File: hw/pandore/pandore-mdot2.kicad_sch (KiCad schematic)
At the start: 15 parts, among them J13 NGFF_M.2_M, J19 NGFF_M.2_AE, M2AE30 M2, M2M110 M2, M2M42 M2, M2M60 M2, M2M80 M2

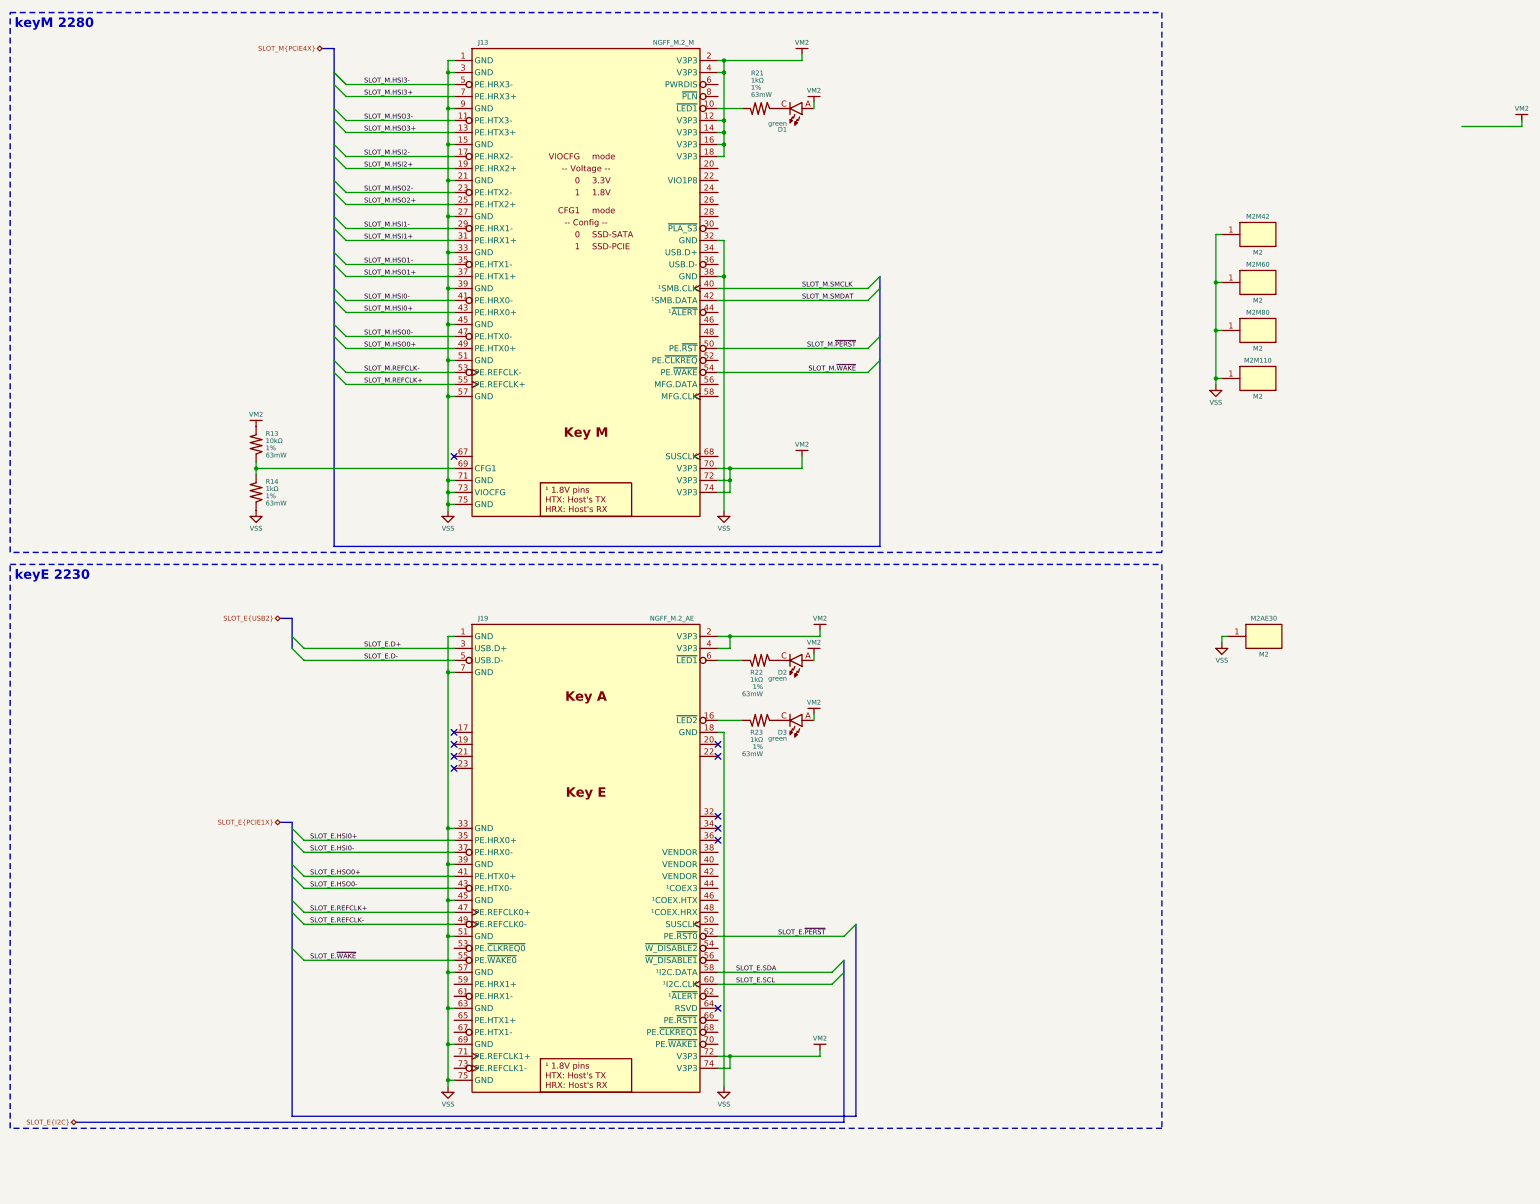
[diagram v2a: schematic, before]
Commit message: most of board control signals added, routed and defined
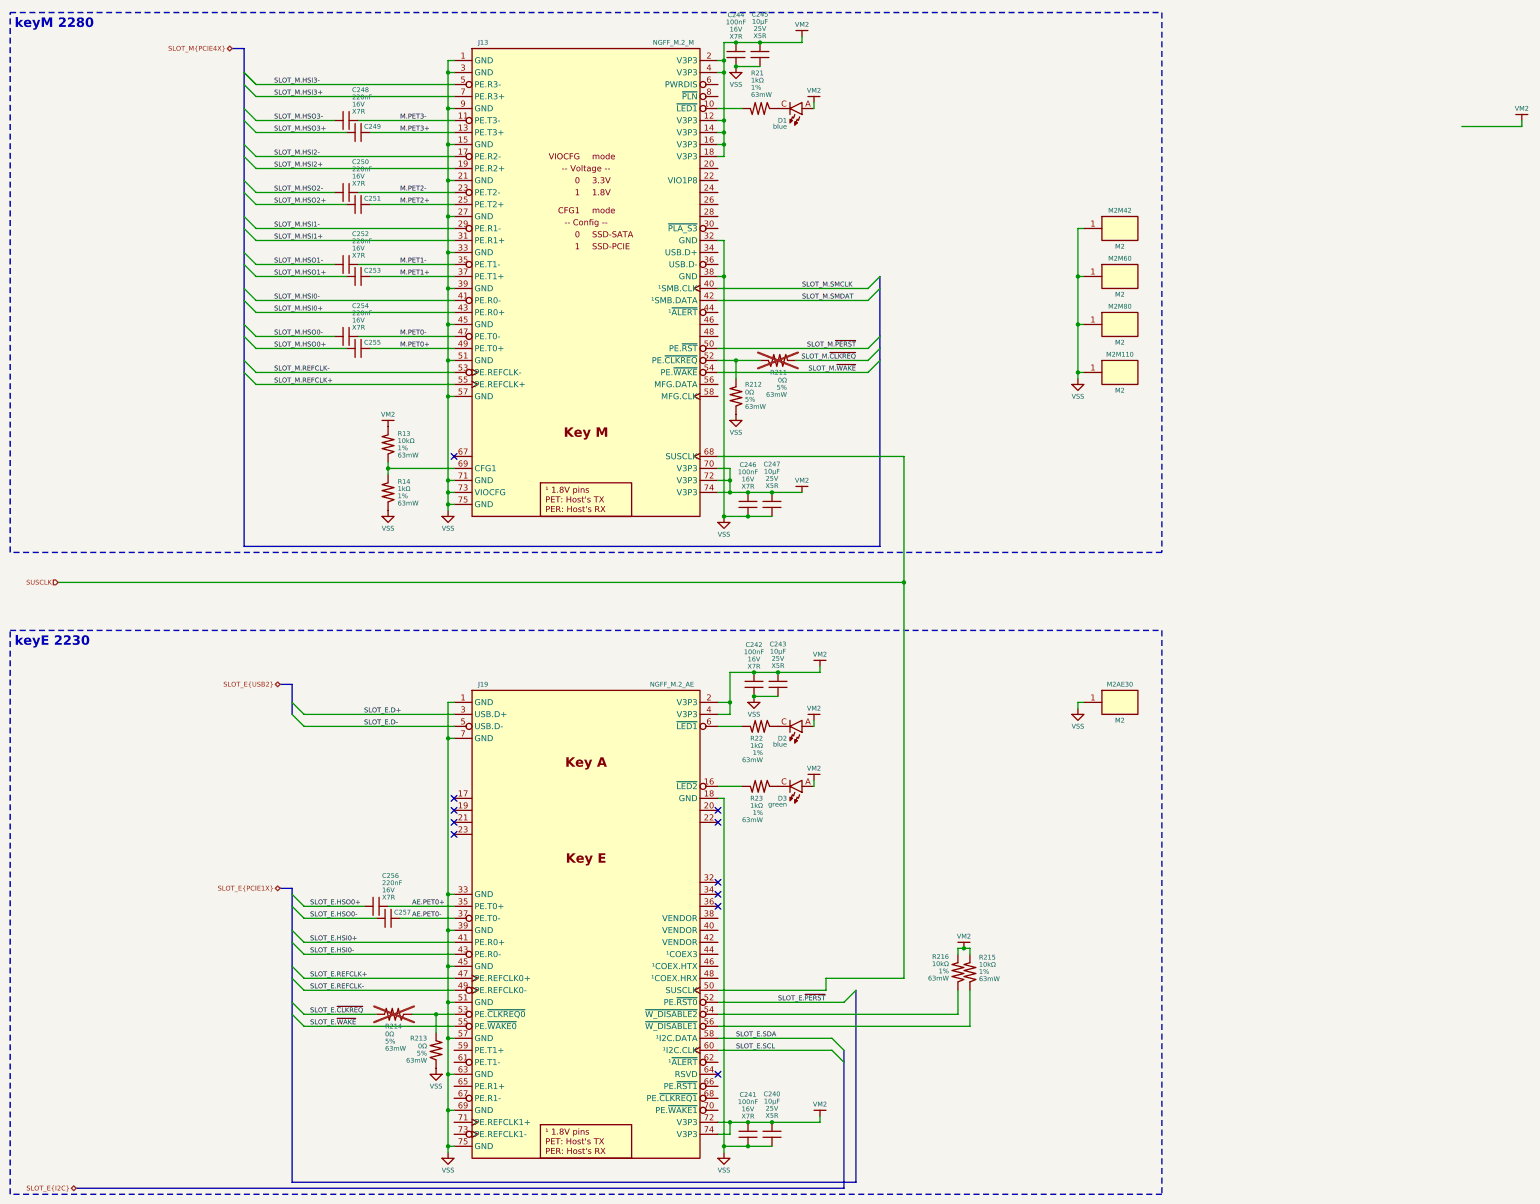
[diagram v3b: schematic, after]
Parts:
- added C240, C243, C245, C247: ${Capacitance}, ${Voltage}, ${Dielectric}, reekilib_cap:CAPC2012, symbol reekilib_cap:cap
- added C241, C242, C244, C246, C248, C249, C250, C251, C252, C253, C254, C255, C256, C257: ${Capacitance}, ${Voltage}, ${Dielectric}, reekilib_cap:CAPC1005, symbol reekilib_cap:cap
- added R211, R212, R213, R214, R215, R216: ${Resistance}, ${Tolerance}, ${Power}, reekilib_res:RESC1005, symbol reekilib_res:res
- D1, D2: Imax 30mA -> 25mA; Link https://ams-osram.com/products/leds/color-leds/osram-smartled-0603-kt-eelp41-12 -> https://ams-osram.com/products/leds/color-leds/osram-smartled-0603-kb-eelp41-12; MPN KT EELP41.12-S2U1-25-2X4Y -> KB EELP41.12-P1R2-36-3X4X; Vf 2.5V -> 2.75V; color green -> blue; lum 224mcd@5mA -> 112mcd@5mA; λdom 527nm -> 470nm
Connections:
- net SLOT_E.HSI0+: now also J19.41 (PE.R0+); no longer J19.35 (PE.HRX0+)
- net SLOT_E.HSI0-: now also J19.43 (PE.R0-); no longer J19.37 (PE.HRX0-)
- net SLOT_E.HSO0+: now also C256.2; no longer J19.41 (PE.HTX0+)
- net SLOT_E.HSO0-: now also C257.2; no longer J19.43 (PE.HTX0-)
- net SLOT_M.HSO0+: now also C255.2; no longer J13.49 (PE.HTX0+)
- net SLOT_M.HSO0-: now also C254.2; no longer J13.47 (PE.HTX0-)
- net SLOT_M.HSO1+: now also C253.2; no longer J13.37 (PE.HTX1+)
- net SLOT_M.HSO1-: now also C252.2; no longer J13.35 (PE.HTX1-)
- net SLOT_M.HSO2+: now also C251.2; no longer J13.25 (PE.HTX2+)
- net SLOT_M.HSO2-: now also C250.2; no longer J13.23 (PE.HTX2-)
- net SLOT_M.HSO3+: now also C249.2; no longer J13.13 (PE.HTX3+)
- net SLOT_M.HSO3-: now also C248.2; no longer J13.11 (PE.HTX3-)
- net VM2: now also C240.2, C241.2, C242.2, C243.2, C244.2, C245.2, C246.2, C247.2, R215.1, R216.1
- net VSS: now also C240.1, C241.1, C242.1, C243.1, C244.1, C245.1, C246.1, C247.1, R212.2, R213.2
- net SUSCLK: now reaches J19.50 (SUSCLK)
- net SUSCLK: now also J13.68 (SUSCLK)
- net at J19.53 (PE.~{CLKREQ0}): now also R213.1, R214.2
- net at J19.54 (~{W_DISABLE2}): now also R216.2
- net at J19.56 (~{W_DISABLE1}): now also R215.2
- net at J13.52 (PE.~{CLKREQ}): now also R211.2, R212.1
- new net AE.PET0+: C256.1, J19.35 (PE.T0+)
- new net AE.PET0-: C257.1, J19.37 (PE.T0-)
- new net M.PET0+: C255.1, J13.49 (PE.T0+)
- new net M.PET0-: C254.1, J13.47 (PE.T0-)
- new net M.PET1+: C253.1, J13.37 (PE.T1+)
- new net M.PET1-: C252.1, J13.35 (PE.T1-)
- new net M.PET2+: C251.1, J13.25 (PE.T2+)
- new net M.PET2-: C250.1, J13.23 (PE.T2-)
- new net M.PET3+: C249.1, J13.13 (PE.T3+)
- new net M.PET3-: C248.1, J13.11 (PE.T3-)
- new net SLOT_E.~{CLKREQ}: R214.1
- new net SLOT_M.~{CLKREQ}: R211.1
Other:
- moved on the sheet: D2, D3, J19, M2AE30, M2M110, M2M42, M2M60, M2M80, R13, R14, R22, R23

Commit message: last sprint almost done, most routing done
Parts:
- added R278, R279, R280, R282: ${Resistance}, ${Tolerance}, ${Power}, reekilib_res:RESC1005, symbol reekilib_res:res
- R13, R14: now not fitted
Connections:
- net VSS: now also R282.1; no longer J13.73 (VIOCFG)
- net SUSCLK: no longer names the net of J19.50 (SUSCLK)
- net SUSCLK: now also R278.2; no longer J13.68 (SUSCLK)
- net VM2 renamed V3P3
- net V3P3: now also R280.1
- new net: J13.68 (SUSCLK), R279.2
- new net: J13.73 (VIOCFG), R280.2, R282.2
- new net SLOT_E.SUSCLK: R278.1
- new net SLOT_M.SUSCLK: R279.1
- no-connect marks 11 -> 42

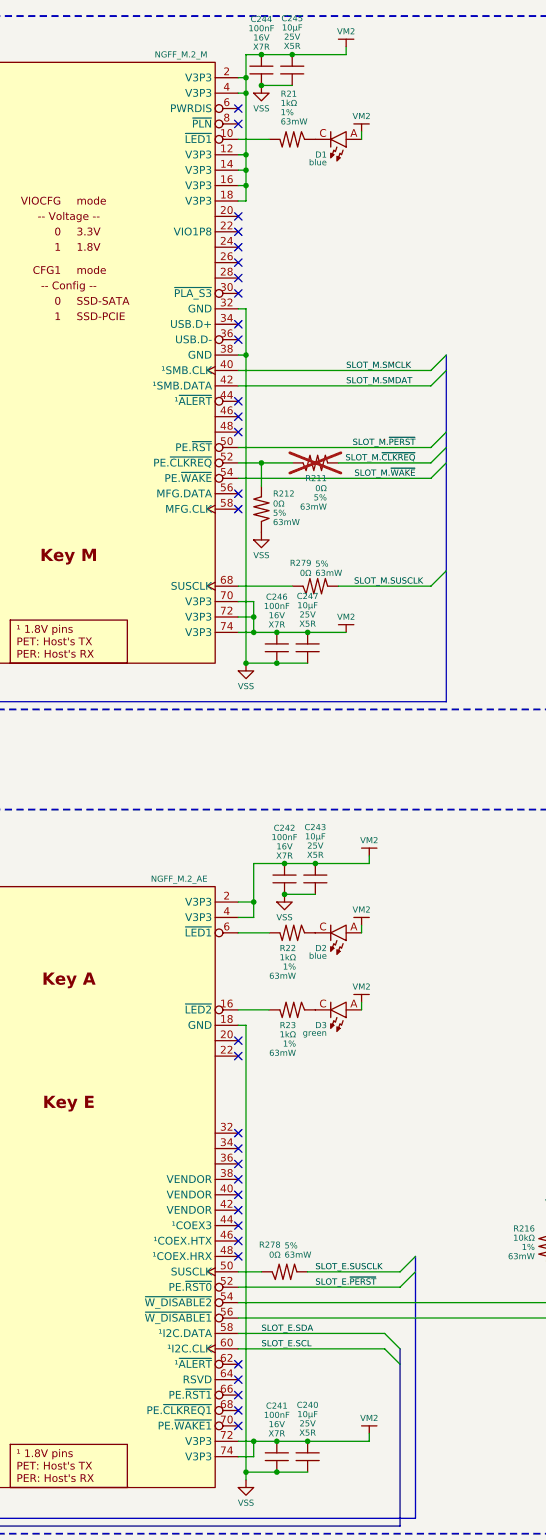
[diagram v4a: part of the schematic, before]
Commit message: finished adding mpn,mfg to all parts, finished routing placement
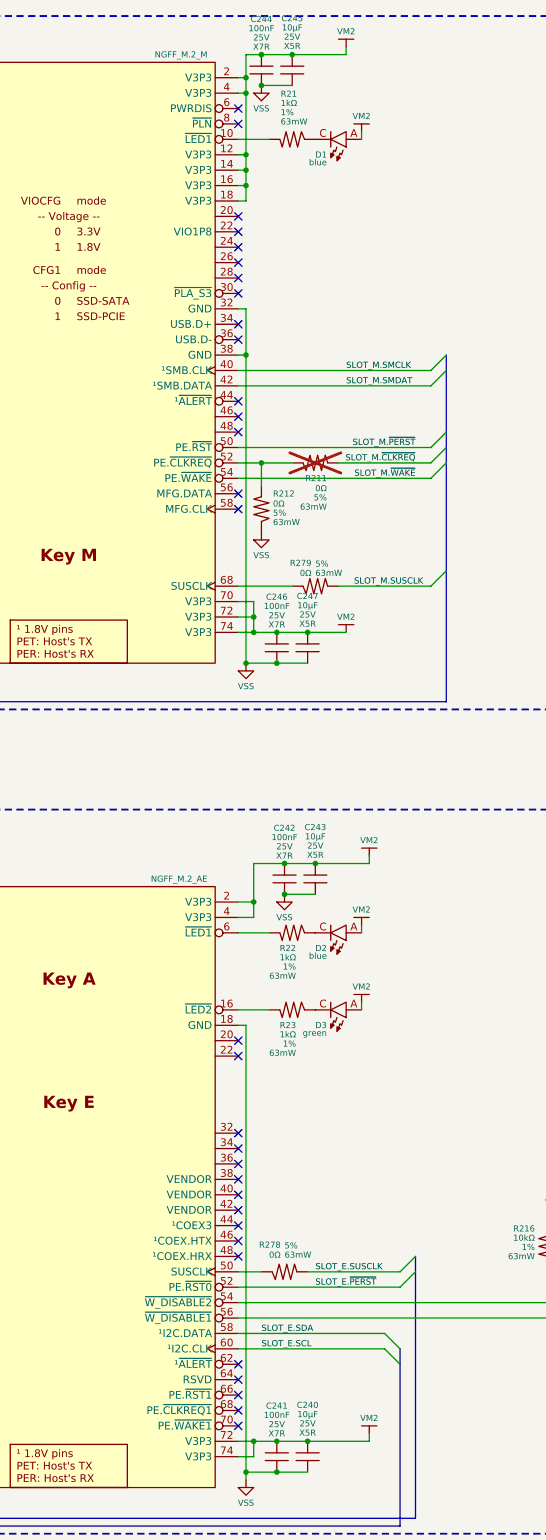
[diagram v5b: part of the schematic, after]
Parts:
- C240, C243, C245, C247: MFG (none) -> Murata; MPN (none) -> GRM21BR61E106KA73K
- C241, C242, C244, C246: MFG2 Samsung Electro-Mechanics -> (none); MFG3 Taiyo Yuden -> (none); MPN2 CL05B104KA5NNNC -> (none); MPN3 EMK105B7104KV-F -> (none); Voltage 16V -> 25V
- C248, C249, C250, C251, C252, C253, C254, C255, C256, C257: MFG (none) -> Murata; MPN (none) -> GRM155R71C224KA12D
- R14, R21, R22, R23: Link (none) -> https://yageogroup.com/products/Resistors/part/RC0402FR-131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; MFG (none) -> YAGEO; MPN (none) -> RC0402FR-131KL
- R211, R212, R213, R214, R278, R279, R282: Link (none) -> https://yageogroup.com/products/Resistors/part/RC0402JR-070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; MFG (none) -> Yageo; MFG2 (none) -> Stackpole; MFG3 (none) -> Vishay Dale; MPN (none) -> RC0402JR-070RL; MPN2 (none) -> RMCF0402ZT0R00; MPN3 (none) -> CRCW04020000Z0ED
